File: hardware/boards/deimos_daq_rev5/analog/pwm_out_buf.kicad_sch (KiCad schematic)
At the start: 3 parts

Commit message: restore rev5 and make this rev rev6
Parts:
- added C56001: 0.1uF, Capacitor_SMD:C_0402_1005Metric, symbol Device:C_Small
- added U56001: 74LVC1G17, Package_TO_SOT_SMD:SOT-23-5, symbol 74xGxx:74LVC1G17
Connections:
- net GND: now also C56001.1, U56001.3 (GND)
- net VIN: now also U56001.2; no longer D56001.1 (K), R56002.1
- new net: D56001.1 (K), R56002.1, U56001.4
- new net +3V3: C56001.2, U56001.5 (VCC)
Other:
- moved on the sheet: D56001, R56001

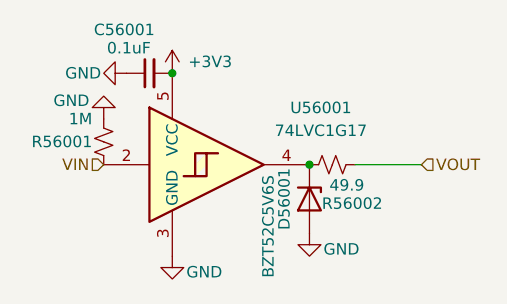
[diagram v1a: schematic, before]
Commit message: remove unnecessary amps and buffers
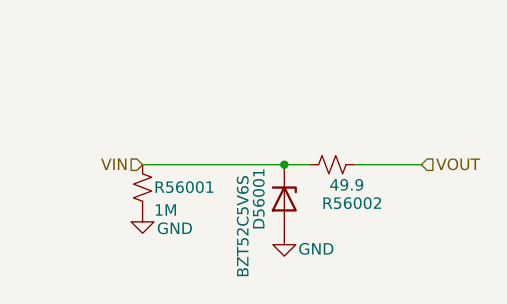
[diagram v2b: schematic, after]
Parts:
- removed C56001: 0.1uF, Capacitor_SMD:C_0402_1005Metric, symbol Device:C_Small
- removed U56001: 74LVC1G17, Package_TO_SOT_SMD:SOT-23-5, symbol 74xGxx:74LVC1G17
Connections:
- net VIN: now also D56001.1 (K), R56002.1
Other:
- moved on the sheet: D56001, R56001
